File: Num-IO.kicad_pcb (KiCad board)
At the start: 2 copper layers, 170.2 x 77.5 mm, 101 parts, among them J1 DB37_Female, J2 DB37_Male, J3 Conn_02x25_Odd_Even, J4 0826-1X1T-GH-F, U1 MAX14917AFM+, U10 LTC6820IUD, U11 LTC6820IUD, U12 LTC6820IUD, U2 MAX14917AFM+, U3 MAX14851AEE+, U4 MAX14917AFM+, U5 MAX31910AUI+, U6 MAX31910AUI+, U7 MAX31910AUI+, U8 MAX31910AUI+, U9 LTC6820IUD

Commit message: routing stuff
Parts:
- C17: value 10nF -> 10nF->
- C6: value 10nF -> <-10nF
- moved R26 160.0 mm to (61.3, 48.3)
- moved R15 155.3 mm to (66.2, 62.0), turned to 180 degrees
- moved C51 146.4 mm to (64.6, 76.6)
- moved C55 146.4 mm to (66.9, 76.6)
- moved R14 146.4 mm to (62.7, 71.2)
- moved R18 146.4 mm to (64.5, 68.7)
- moved R22 146.4 mm to (66.8, 68.0)
- moved U11 146.4 mm to (66.0, 72.6)
- moved C52 144.2 mm to (69.0, 57.7), turned to 90 degrees
- moved R24 142.3 mm to (81.2, 46.9), turned to 90 degrees
- moved R21 138.9 mm to (76.4, 69.2)
- moved C49 134.5 mm to (83.4, 59.1)
- moved C53 128.6 mm to (83.5, 61.4)
- moved C54 118.5 mm to (84.4, 74.8)
- moved C21 74.7 mm to (151.8, 67.2)
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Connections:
- net Net-(J4-Pad10) renamed /RJ45 extension/TRD1-
- net Net-(J4-Pad11) renamed /RJ45 extension/TRD1+
- net Net-(J4-Pad2) renamed /RJ45 extension/TRD3-
- net Net-(J4-Pad3) renamed /RJ45 extension/TRD3+
- net Net-(J4-Pad4) renamed /RJ45 extension/TRD2+
- net Net-(J4-Pad5) renamed /RJ45 extension/TRD2-
- net Net-(J4-Pad8) renamed /RJ45 extension/TRD4+
- net Net-(J4-Pad9) renamed /RJ45 extension/TRD4-
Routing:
- net /FPGA Connector/SPI1.SDI: track 0.00 -> 118.9 mm
- net /FPGA Connector/SPI1.CLK: track 0.00 -> 114.9 mm
- net +24V: track 0.00 -> 112.2 mm
- net GNDD: track 0.00 -> 109.4 mm
- net /FPGA Connector/SPI1.*CS: track 0.00 -> 104.7 mm
- net /FPGA Connector/SPI1.SDO: track 0.00 -> 88.4 mm, vias 0 -> 1
- net /FPGA Connector/SPI2.*CS: track 0.00 -> 82.5 mm, vias 0 -> 1
- net /FPGA Connector/SPI2.SDI: track 0.00 -> 81.7 mm, vias 0 -> 1
- net /FPGA Connector/SPI2.CLK: track 0.00 -> 77.7 mm, vias 0 -> 1
- net /FPGA Connector/SPI2.SDO: track 0.00 -> 77.3 mm, vias 0 -> 1
- net OUTPWR: track 4.93 -> 79.4 mm
- net /SDI: track 0.00 -> 72.7 mm, vias 0 -> 2
- net /FPGA Connector/SPI3.SDO: track 0.00 -> 72.4 mm
- net /*FAULT: track 78.7 -> 145.5 mm, vias 6 -> 9
- net /CS: track 76.3 -> 143.0 mm, vias 6 -> 9
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
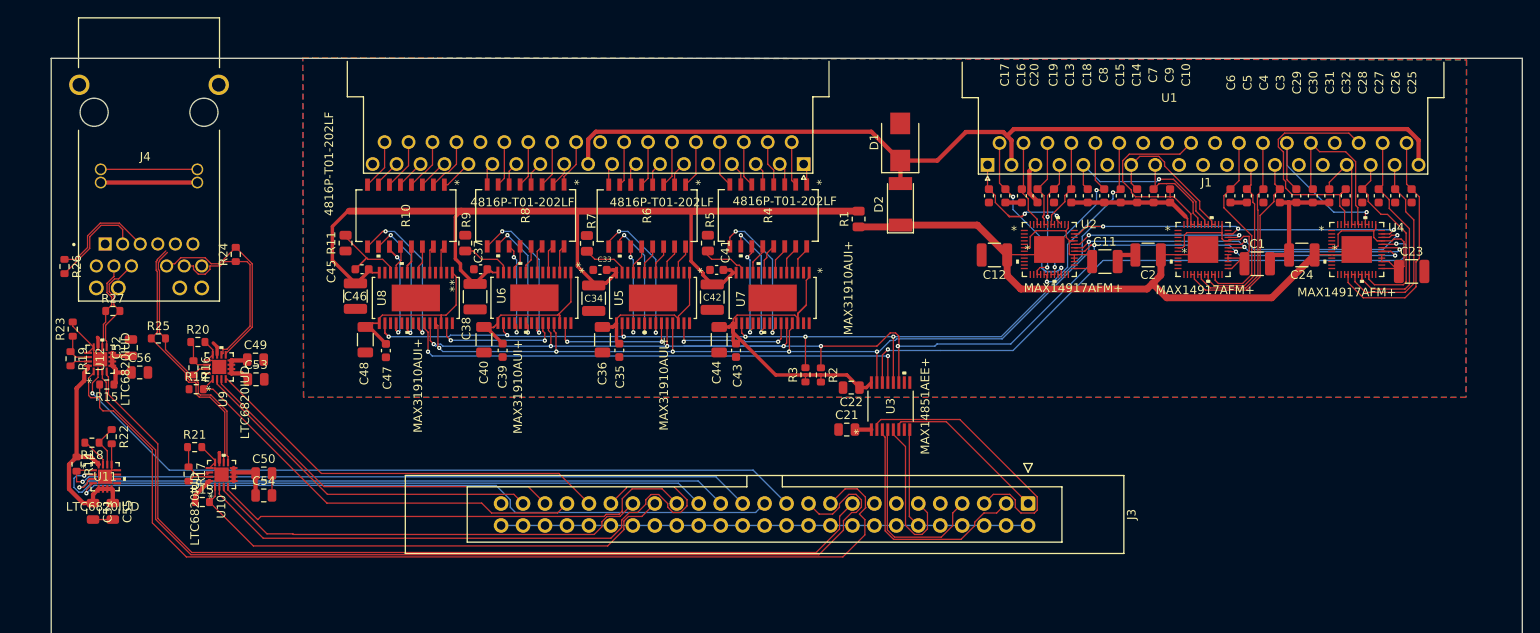
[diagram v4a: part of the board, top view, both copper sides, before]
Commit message: Basic routing done, cheating a bit on the diff + add holes (to be positionned)
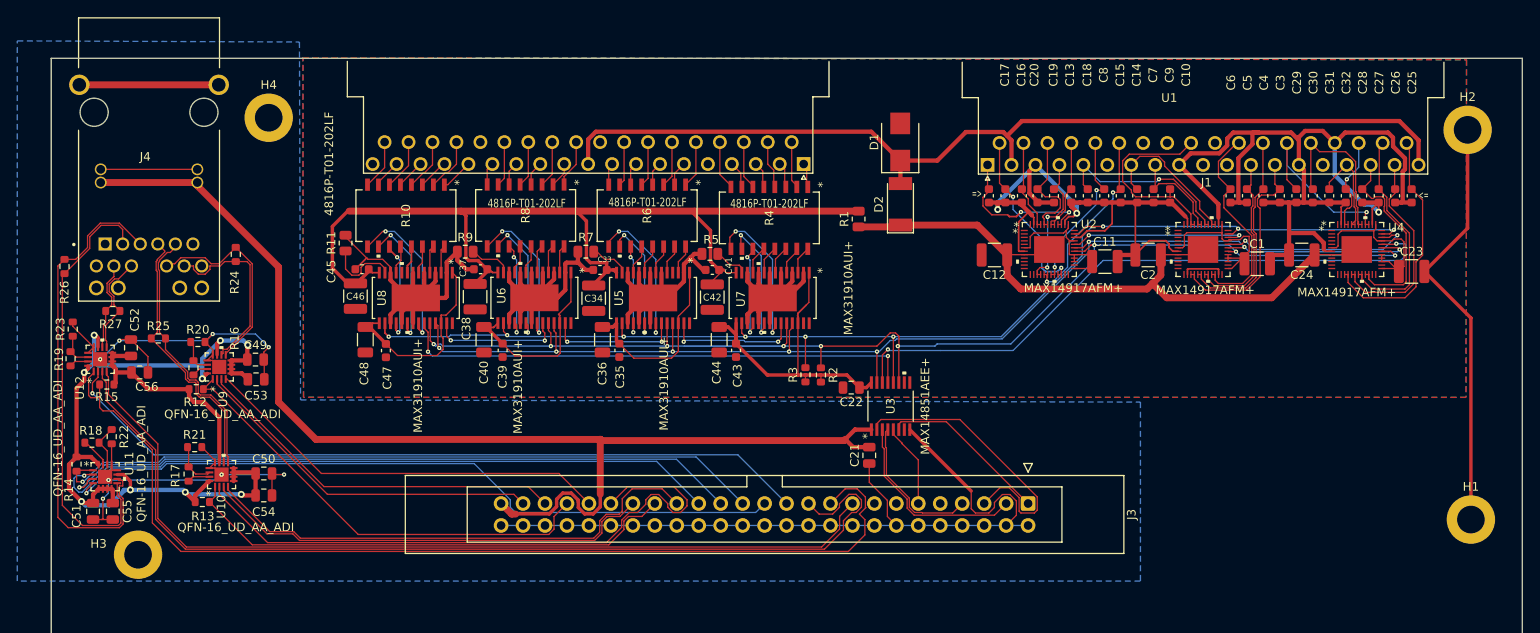
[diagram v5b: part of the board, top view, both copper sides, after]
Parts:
- added H1: MountingHole_Pad, MountingHole:MountingHole_3.2mm_M3_DIN965_Pad, F.Cu at (224.0, 77.6)
- added H2: MountingHole_Pad, MountingHole:MountingHole_3.2mm_M3_DIN965_Pad, F.Cu at (223.6, 32.5)
- added H3: MountingHole_Pad, MountingHole:MountingHole_3.2mm_M3_DIN965_Pad, F.Cu at (69.8, 81.7)
- added H4: MountingHole_Pad, MountingHole:MountingHole_3.2mm_M3_DIN965_Pad, F.Cu at (85.0, 31.1)
- C17: value 10nF-> -> 10nF
- C6: value <-10nF -> 10nF
- U10, U11, U12, U9: value LTC6820IUD -> QFN-16_UD_AA_ADI
- moved C21 3.96 mm to (154.4, 70.2), turned to 90 degrees
- moved R5 1.27 mm to (136.0, 46.9), turned to 0 degrees
- moved R9 0.99 mm to (107.7, 46.6), turned to 0 degrees
- moved R7 0.97 mm to (121.6, 46.6), turned to 0 degrees
- moved C41 0.50 mm to (136.3, 48.7)
- moved R4 0.31 mm to (142.9, 42.7)
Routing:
- net GNDPWR: track 49.1 -> 401.2 mm, vias 0 -> 3
- net +5VD: track 13.1 -> 137.7 mm
- net GNDD: track 109.4 -> 188.7 mm, vias 0 -> 8
- net +3.3V: track 53.8 -> 126.1 mm, vias 0 -> 9
- net /RJ45 extension/TRD3+: track 12.3 -> 57.0 mm
- net /RJ45 extension/TRD3-: track 11.7 -> 51.3 mm
- net /output channel 1-8/OUT5: track 28.6 -> 11.2 mm, vias 0 -> 1
- net Earth: track 0.00 -> 16.1 mm
- net Net-(R11-Pad2): track 0.00 -> 8.60 mm
- net /I*FAULT: track 18.3 -> 9.74 mm
- net /FPGA Connector/SPI0.SDO: track 23.1 -> 17.1 mm
- net /FPGA Connector/SPI0.SDI: track 28.2 -> 22.6 mm
- net /output channel 17-24/OUT8: track 14.1 -> 18.0 mm
- net INPWR: track 114.1 -> 111.0 mm
- net /input channel 17-24/5VOUT: track 18.6 -> 21.7 mm
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- added copper zone on B.Cu, net GNDD
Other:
- board text added: "=>"

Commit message: before switching packaging
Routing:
- added copper zone on F.Cu, net +24V

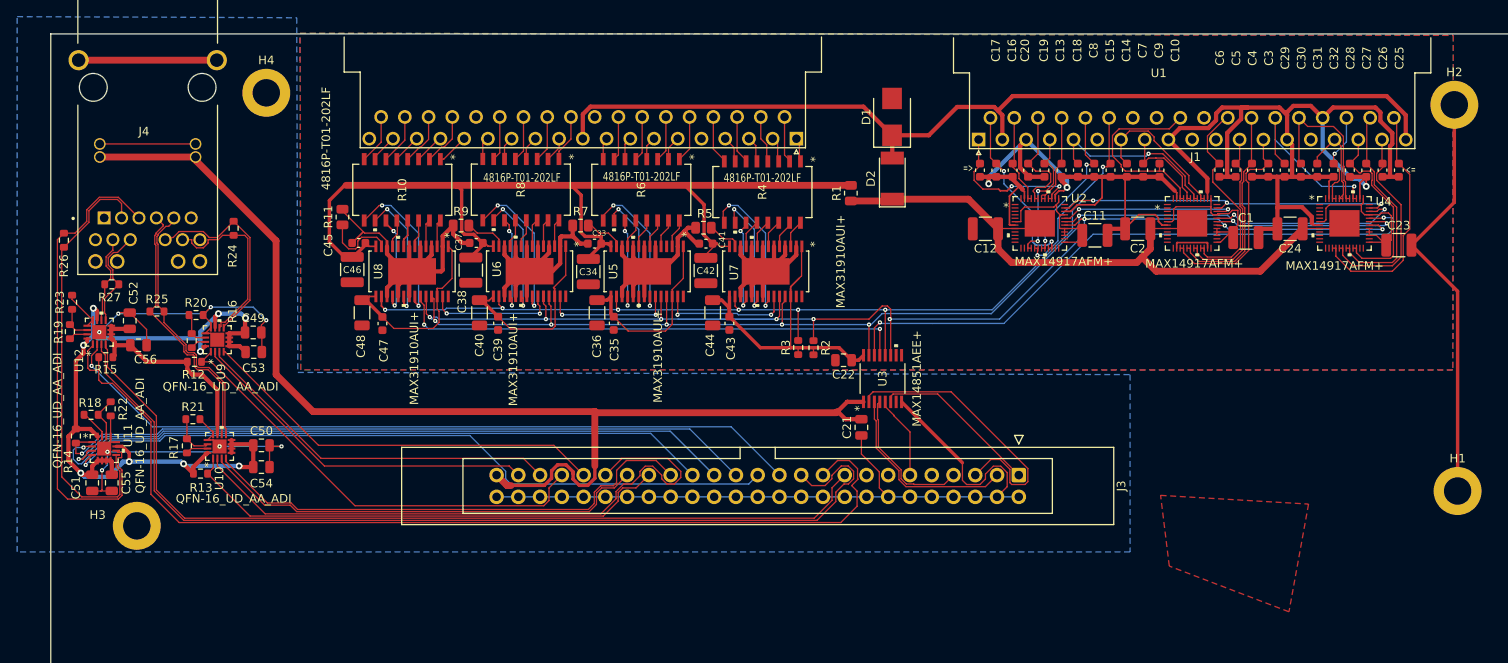
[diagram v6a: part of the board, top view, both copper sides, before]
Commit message: change package QFN => MSOP
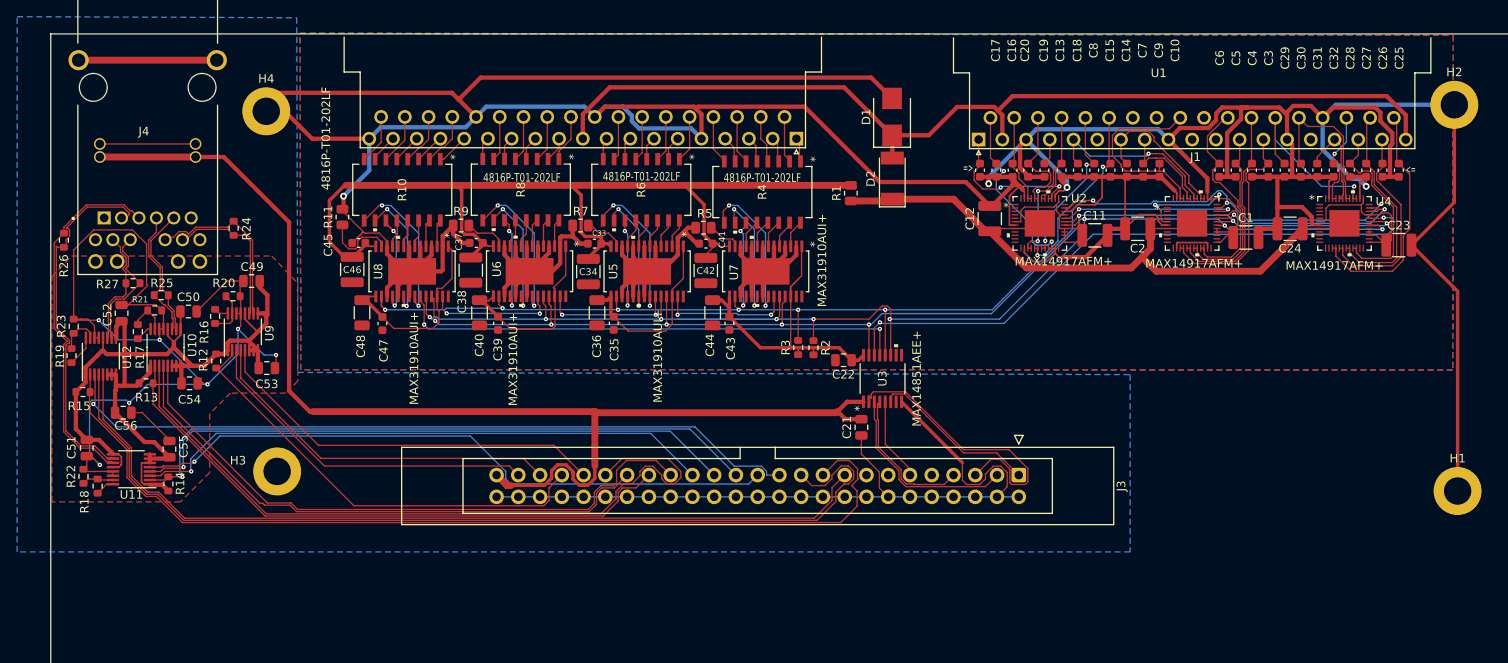
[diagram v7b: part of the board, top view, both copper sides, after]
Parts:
- U10, U11, U12, U9: value QFN-16_UD_AA_ADI -> LTC6820HMS; footprint Maxim industrial IO:LTC6820IUD -> Package_SO:MSOP-16_3x4.039mm_P0.5mm
- moved C50 17.8 mm to (75.9, 56.6)
- moved H3 17.6 mm to (86.2, 75.3)
- moved R17 14.5 mm to (70.0, 59.0)
- moved R21 13.5 mm to (71.9, 56.5)
- moved U10 13.2 mm to (73.2, 60.8)
- moved C54 12.9 mm to (76.0, 65.0)
- moved R13 12.3 mm to (70.9, 65.0)
- moved R14 12.2 mm to (73.5, 76.8), turned to 90 degrees
- moved R22 8.49 mm to (63.6, 75.9), turned to 90 degrees
- moved R18 8.36 mm to (65.3, 77.0), turned to -90 degrees
- moved C56 8.07 mm to (68.3, 68.5)
- moved C55 7.80 mm to (73.7, 72.7), turned to 90 degrees
- moved C49 6.01 mm to (83.2, 53.1), turned to 180 degrees
- moved R15 4.86 mm to (63.6, 66.0), turned to 0 degrees
- moved R20 4.85 mm to (81.1, 54.9)
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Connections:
- H3 pad 1: GNDPWR -> (no net)
- U10 pad 1: /FPGA Connector/SPI3.SDI -> +3.3V
- U10 pad 10: /RJ45 extension/TRD2+ -> /RJ45 extension/TRD2-
- U10 pad 11: +3.3V -> /RJ45 extension/TRD2+
- U10 pad 12: GNDD -> +3.3V
- U10 pad 14: Net-(R17-Pad1) -> GNDD
- U10 pad 15: Net-(R17-Pad2) -> Net-(R17-Pad1)
- U10 pad 16: +3.3V -> Net-(R17-Pad2)
- U10 pad 2: /FPGA Connector/SPI3.SDO -> /FPGA Connector/SPI3.SDI
- U10 pad 3: /FPGA Connector/SPI3.CLK -> /FPGA Connector/SPI3.SDO
- U10 pad 4: /FPGA Connector/SPI3.*CS -> /FPGA Connector/SPI3.CLK
- U10 pad 5: +3.3V -> /FPGA Connector/SPI3.*CS
- U10 pad 9: /RJ45 extension/TRD2- -> +3.3V
- U11 pad 1: /FPGA Connector/SPI2.SDI -> +3.3V
- U11 pad 10: /RJ45 extension/TRD3+ -> /RJ45 extension/TRD3-
- U11 pad 11: +3.3V -> /RJ45 extension/TRD3+
- U11 pad 12: GNDD -> +3.3V
- U11 pad 14: Net-(R18-Pad1) -> GNDD
- U11 pad 15: Net-(R18-Pad2) -> Net-(R18-Pad1)
- U11 pad 16: +3.3V -> Net-(R18-Pad2)
- U11 pad 2: /FPGA Connector/SPI2.SDO -> /FPGA Connector/SPI2.SDI
- U11 pad 3: /FPGA Connector/SPI2.CLK -> /FPGA Connector/SPI2.SDO
- U11 pad 4: /FPGA Connector/SPI2.*CS -> /FPGA Connector/SPI2.CLK
- U11 pad 5: +3.3V -> /FPGA Connector/SPI2.*CS
- U11 pad 9: /RJ45 extension/TRD3- -> +3.3V
- U12 pad 1: /FPGA Connector/SPI1.SDI -> +3.3V
- U12 pad 10: /RJ45 extension/TRD4+ -> /RJ45 extension/TRD4-
- U12 pad 11: +3.3V -> /RJ45 extension/TRD4+
- U12 pad 12: GNDD -> +3.3V
- U12 pad 14: Net-(R19-Pad1) -> GNDD
- U12 pad 15: Net-(R19-Pad2) -> Net-(R19-Pad1)
- U12 pad 16: +3.3V -> Net-(R19-Pad2)
- U12 pad 2: /FPGA Connector/SPI1.SDO -> /FPGA Connector/SPI1.SDI
- U12 pad 3: /FPGA Connector/SPI1.CLK -> /FPGA Connector/SPI1.SDO
- U12 pad 4: /FPGA Connector/SPI1.*CS -> /FPGA Connector/SPI1.CLK
- U12 pad 5: +3.3V -> /FPGA Connector/SPI1.*CS
- U12 pad 9: /RJ45 extension/TRD4- -> +3.3V
- U9 pad 1: /FPGA Connector/SPI4.SDI -> +3.3V
- U9 pad 10: /RJ45 extension/TRD1+ -> /RJ45 extension/TRD1-
- U9 pad 11: +3.3V -> /RJ45 extension/TRD1+
- U9 pad 12: GNDD -> +3.3V
- U9 pad 14: Net-(R16-Pad1) -> GNDD
- U9 pad 15: Net-(R16-Pad2) -> Net-(R16-Pad1)
- U9 pad 16: +3.3V -> Net-(R16-Pad2)
- U9 pad 2: /FPGA Connector/SPI4.SDO -> /FPGA Connector/SPI4.SDI
- U9 pad 3: /FPGA Connector/SPI4.CLK -> /FPGA Connector/SPI4.SDO
- U9 pad 4: /FPGA Connector/SPI4.*CS -> /FPGA Connector/SPI4.CLK
- U9 pad 5: +3.3V -> /FPGA Connector/SPI4.*CS
- U9 pad 9: /RJ45 extension/TRD1- -> +3.3V
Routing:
- net GNDPWR: track 401.2 -> 653.6 mm, vias 3 -> 4
- net GNDD: track 188.7 -> 229.9 mm, vias 8 -> 7
- net +3.3V: track 126.1 -> 107.6 mm, vias 9 -> 0
- net /RJ45 extension/TRD2+: track 31.1 -> 15.2 mm
- net /RJ45 extension/TRD2-: track 30.8 -> 15.3 mm
- net /RJ45 extension/TRD3+: track 57.0 -> 42.9 mm
- net /FPGA Connector/SPI3.CLK: track 52.7 -> 66.5 mm
- net /FPGA Connector/SPI3.*CS: track 59.3 -> 72.9 mm
- net /FPGA Connector/SPI3.SDO: track 72.9 -> 86.4 mm
- net /FPGA Connector/SPI3.SDI: track 58.2 -> 70.4 mm
- net /FPGA Connector/SPI2.SDO: track 79.4 -> 68.3 mm
- net /FPGA Connector/SPI2.*CS: track 84.6 -> 75.7 mm
- net /RJ45 extension/TRD3-: track 51.3 -> 43.0 mm
- net /FPGA Connector/SPI2.CLK: track 79.8 -> 71.8 mm
- net /FPGA Connector/SPI2.SDI: track 83.6 -> 76.0 mm
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- added copper zone on F.Cu, net +3.3V
- removed copper zone on F.Cu, net +24V
